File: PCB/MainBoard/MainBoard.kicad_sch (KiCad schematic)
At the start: 136 parts, among them J1 Fan, J2 PowerIn, J3 AuxPowerIn, J4 LCD Display, J5 SWD, J6 FrontPanel, J7 PowerOut, K1 OUT_A_ENABLE_RELAY, K2 OUT_B_ENABLE_RELAY, K3 Relay_SPDT_Panasonic_ALQ105, K4 Relay_SPDT_Panasonic_ALQ105, K5 Relay_SPDT_Panasonic_ALQ105, M1 Fan, Q1 TIP41C, Q10 2N2222, Q11 TIP41C, Q12 TIP41C, Q2 TSM2302CX, Q3 TIP41C, Q4 TSM2302CX, Q5 TSM2302CX, Q6 TSM2302CX, Q7 TSM2302CX, Q8 TSM2302CX, Q9 2N2222, U1 LTC2631CTS8-HZ12, U10 LM35-NEB, U2 LTC2631CTS8-HZ12, U3 MCP3428, U4 2SC5200NS1_E_S, U5 LT1490CN8PBF, U6 2SC5200NS1_E_S, U7 STM32F411RETx, U8 MCP1703A-3302_SOT223, U9 LM35-NEB, Y1 24MHz, Y2 32k768

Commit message: Fix minor issues in PCB
Fixed decoupling capacitors connectivbity
Added test points to several networks
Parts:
- added TP1: TP_CH_A_MAINPWR_CTRL, TestPoint:TestPoint_THTPad_D2.0mm_Drill1.0mm, symbol Connector:TestPoint
- added TP10: TP_CH_B_MAINPWR_CTRL, TestPoint:TestPoint_THTPad_D2.0mm_Drill1.0mm, symbol Connector:TestPoint
- added TP13: OPAMP_CH_B_INV, TestPoint:TestPoint_THTPad_D2.0mm_Drill1.0mm, symbol Connector:TestPoint
- added TP3: TP_DAC_VOUT_CH_A, TestPoint:TestPoint_THTPad_D2.0mm_Drill1.0mm, symbol Connector:TestPoint
- added TP5: TP_DAC_VOUT_CH_B, TestPoint:TestPoint_THTPad_D2.0mm_Drill1.0mm, symbol Connector:TestPoint
- added TP8: OPAMP_CH_A_INV, TestPoint:TestPoint_THTPad_D2.0mm_Drill1.0mm, symbol Connector:TestPoint
- renumbered TP6 to TP11, TP7 to TP12, TP8 to TP14, TP9 to TP15, TP10 to TP16, TP1 to TP2, TP2 to TP4, TP3 to TP6, TP4 to TP7, TP5 to TP9
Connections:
- net CH_A_INV: now reaches R16.1, RV1.2, RV1.3, U5.2 (-INA)
- net CH_A_INV: now also TP8.1
- net DAC_VOUT_CH_A: now reaches U1.7 (VOUT), U5.3 (+INA)
- net DAC_VOUT_CH_A: now also TP3.1
- net DAC_VOUT_CH_B: now reaches U2.7 (VOUT), U5.5 (+INB)
- net DAC_VOUT_CH_B: now also TP5.1
- net CH_B_INV: now reaches R20.1, RV2.1, RV2.2, U5.6 (-INB)
- net CH_B_INV: now also TP13.1
- net at C4.2, Q1.3 (E), R4.1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: now also TP1.1
- net at C11.2, Q3.3 (E), R18.1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: now also TP10.1

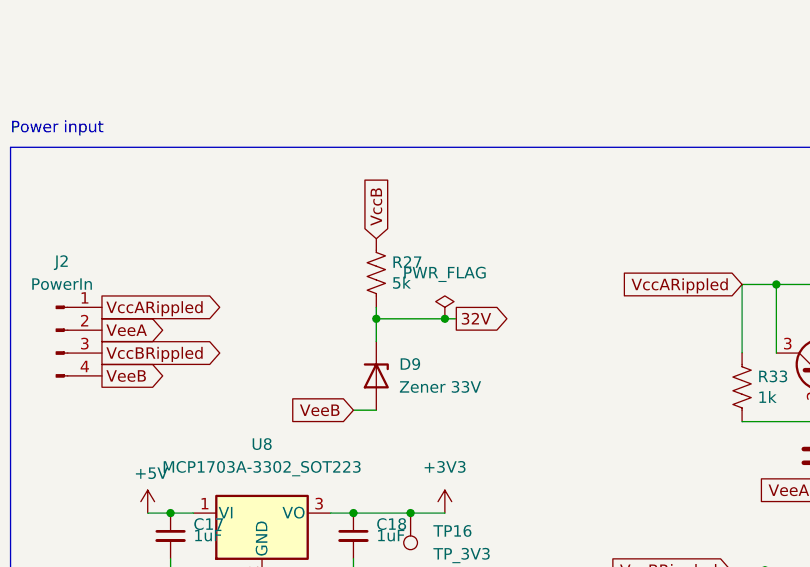
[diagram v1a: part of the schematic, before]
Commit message: Change 33V input resistor value
The previous 5k1 ohm value was completely wrong.
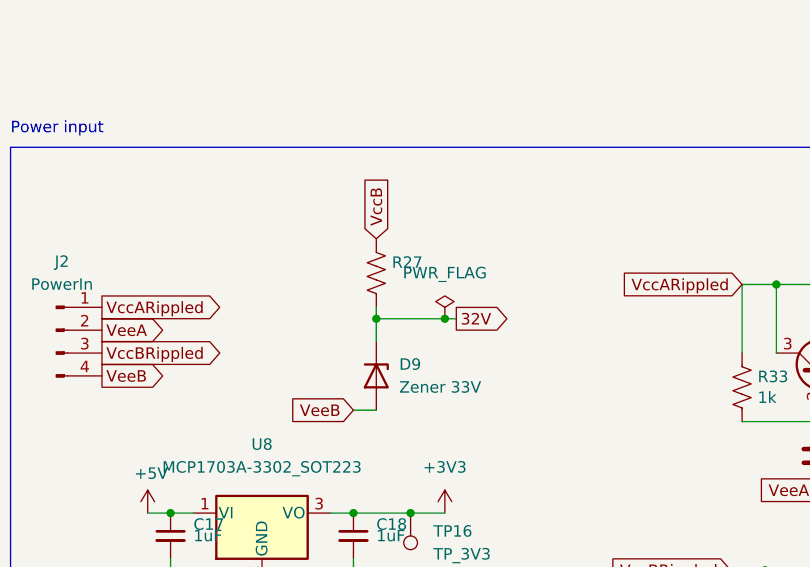
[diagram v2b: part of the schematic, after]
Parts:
- R27: value 5k -> (none); footprint Resistor_THT:R_Axial_DIN0207_L6.3mm_D2.5mm_P10.16mm_Horizontal -> (none)
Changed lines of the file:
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@@
       (effects (font (size 1.27 1.27)) (justify left))
     )
-    (property "Value" "5k" (id 1) (at 319.2272 199.263 0)
-      (effects (font (size 1.27 1.27)) (justify left))
-    )
-    (property "Footprint" "Resistor_THT:R_Axial_DIN0207_L6.3mm_D2.5mm_P10.16mm_Horizontal" (id 2) (at 318.516 198.374 90)
+    (property "Value" "" (id 1) (at 319.2272 199.263 0)
+      (effects (font (size 1.27 1.27)) (justify left))
+    )
+    (property "Footprint" "" (id 2) (at 318.516 198.374 90)
       (effects (font (size 1.27 1.27)) hide)
     )
@@
     )
     (path "/da3fa43c-fb99-4d3d-85d2-ad3d29a37681"
-      (reference "R27") (unit 1) (value "5k") (footprint "Resistor_THT:R_Axial_DIN0207_L6.3mm_D2.5mm_P10.16mm_Horizontal")
+      (reference "R27") (unit 1) (value "100") (footprint "Resistor_THT:R_Axial_DIN0207_L6.3mm_D2.5mm_P10.16mm_Horizontal")
     )
     (path "/00000000-0000-0000-0000-00005f1d9035"
